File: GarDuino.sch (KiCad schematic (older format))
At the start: 15 parts

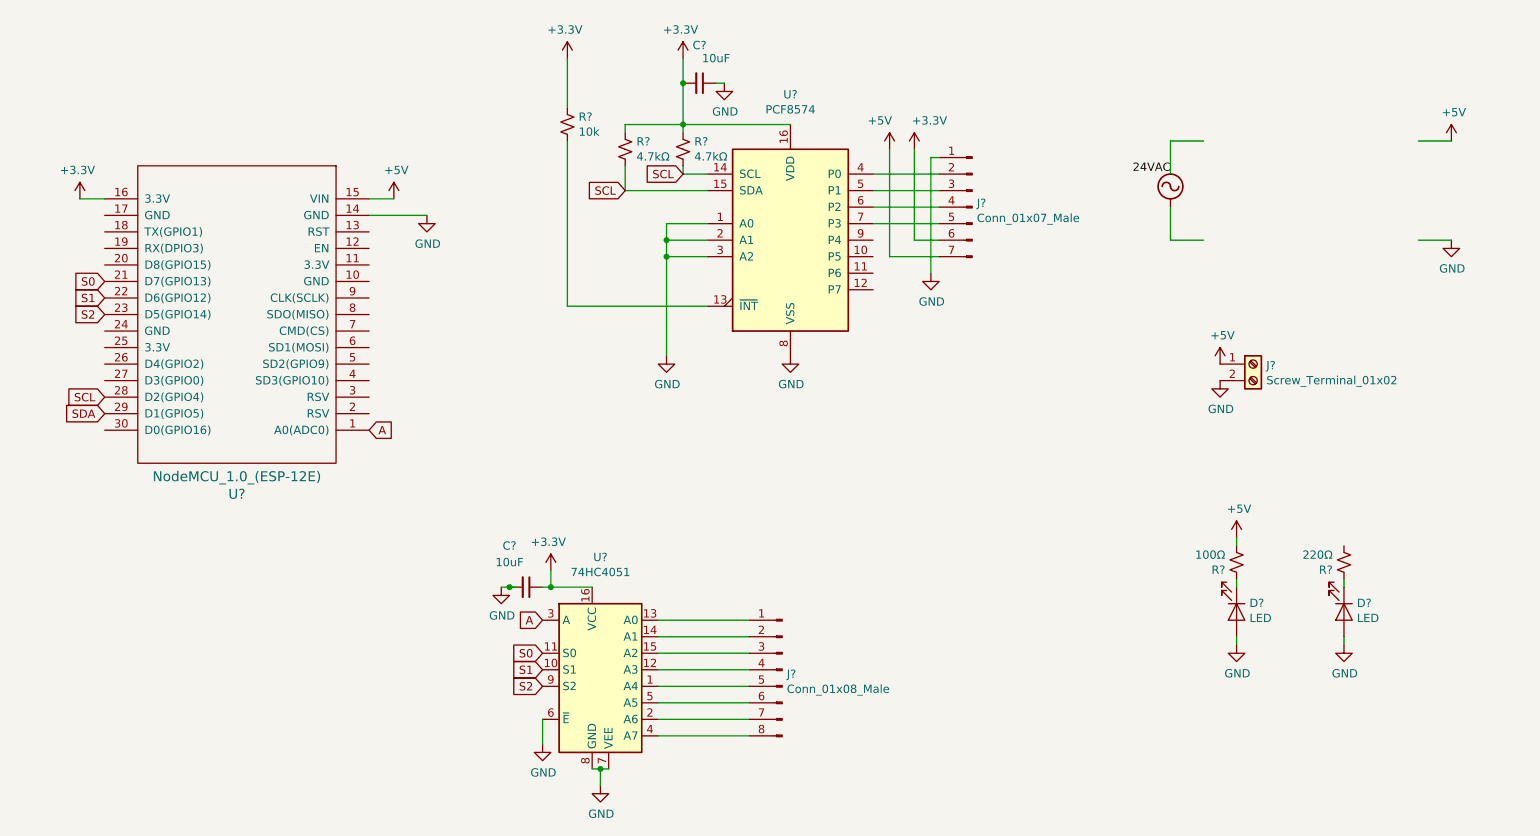
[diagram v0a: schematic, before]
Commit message: Changed schematic to reflect protoboard
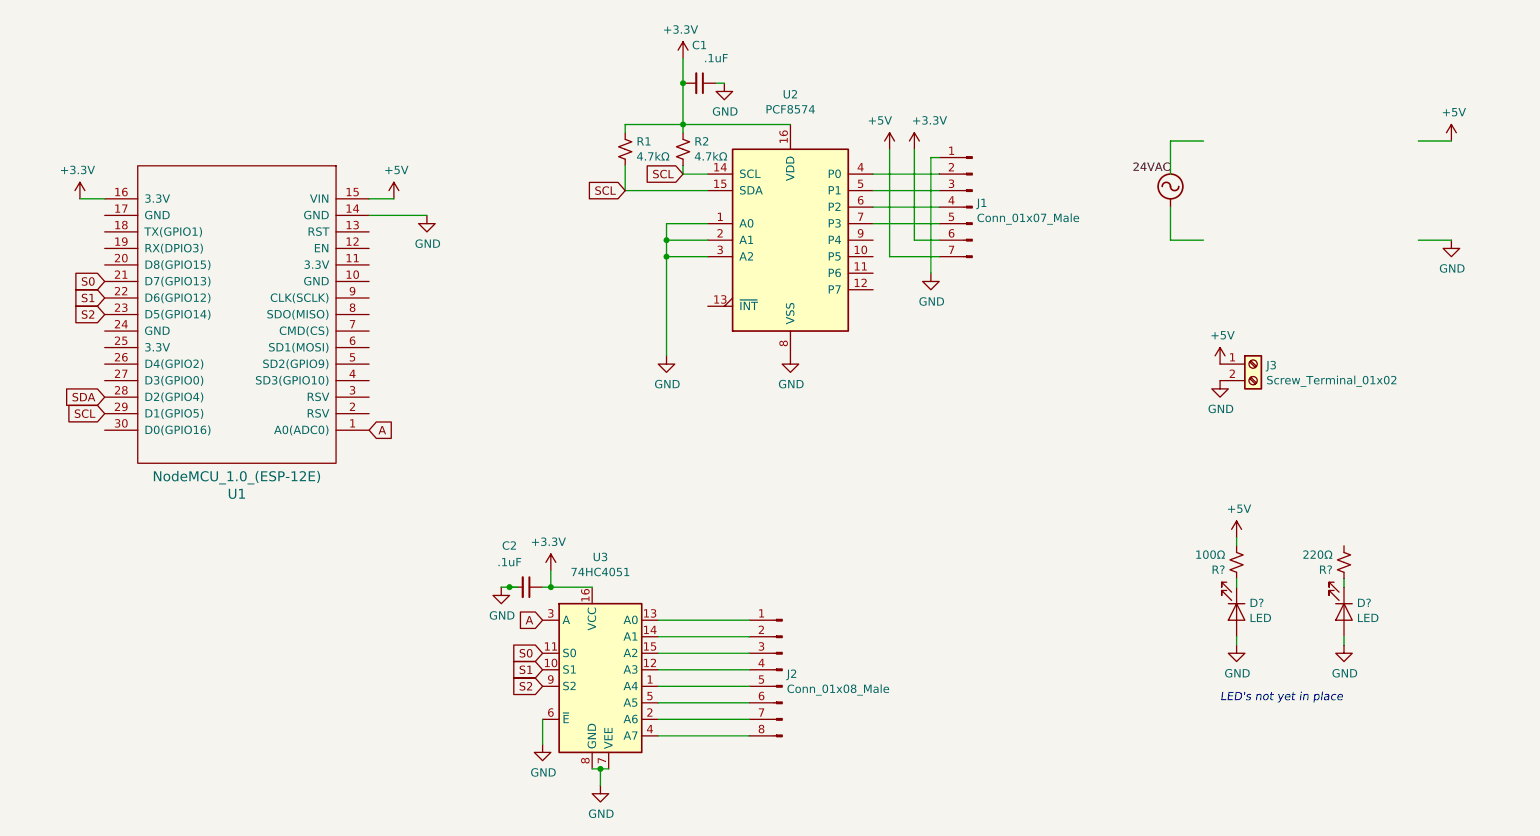
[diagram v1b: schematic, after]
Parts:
- removed R?: 10k, symbol Device:R_Small_US
- C1, C2: renamed from C?; value 10uF -> .1uF
- gave numbers to parts that had none: 8
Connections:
- wire segments 61 -> 58
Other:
- note added: "LED's not yet in place"
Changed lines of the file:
@@
 encoding utf-8
 Sheet 1 1
-Title "Arduino-Based Irrigation Controller"
-Date "2020-04-18"
-Rev "0"
+Title "GarDuino- Arduino-Based Drip Irrigation System"
+Date "2020-04-20"
+Rev "0.1"
 Comp ""
 Comment1 ""
@@
 $EndDescr
 $Comp
-L NodeMCU:NodeMCU_1.0_(ESP-12E) U?
+L NodeMCU:NodeMCU_1.0_(ESP-12E) U1
 U 1 1 5E9944EE
 P 2300 3050
-F 0 "U?" H 2300 4137 60  0000 C CNN
+F 0 "U1" H 2300 4137 60  0000 C CNN
 F 1 "NodeMCU_1.0_(ESP-12E)" H 2300 4031 60  0000 C CNN
 F 2 "" H 1700 2200 60  0000 C CNN
@@
 $EndComp
 $Comp
-L Interface_Expansion:PCF8574 U?
+L Interface_Expansion:PCF8574 U2
 U 1 1 5E99C333
 P 5650 2600
-F 0 "U?" H 5650 3481 50  0000 C CNN
+F 0 "U2" H 5650 3481 50  0000 C CNN
 F 1 "PCF8574" H 5650 3390 50  0000 C CNN
 F 2 "" H 5650 2600 50  0001 C CNN
@@
 $EndComp
 $Comp
-L Device:R_Small_US R?
+L Device:R_Small_US R2
 U 1 1 5E9A68B6
 P 5000 2050
-F 0 "R?" H 5068 2096 50  0000 L CNN
+F 0 "R2" H 5068 2096 50  0000 L CNN
 F 1 "4.7kΩ" H 5068 2005 50  0000 L CNN
 F 2 "" H 5000 2050 50  0001 C CNN
@@
 $EndComp
 $Comp
-L Device:R_Small_US R?
+L Device:R_Small_US R1
 U 1 1 5E9A8484
 P 4650 2050
-F 0 "R?" H 4718 2096 50  0000 L CNN
+F 0 "R1" H 4718 2096 50  0000 L CNN
 F 1 "4.7kΩ" H 4718 2005 50  0000 L CNN
 F 2 "" H 4650 2050 50  0001 C CNN
@@
 	1    0    0    -1
 $EndComp
-$Comp
-L Device:R_Small_US R?
-U 1 1 5E9ABDB9
-P 4300 1900
-F 0 "R?" H 4368 1946 50  0000 L CNN
-F 1 "10k" H 4368 1855 50  0000 L CNN
-F 2 "" H 4300 1900 50  0001 C CNN
-F 3 "~" H 4300 1900 50  0001 C CNN
-	1    4300 1900
-	1    0    0    -1
-$EndComp
 Wire Wire Line
 	4900 2700 4900 3300
@@
 $EndComp
 $Comp
-L 74xx:74HC4051 U?
+L 74xx:74HC4051 U3
 U 1 1 5E9F278B
 P 4450 5200
-F 0 "U?" H 4500 5881 50  0000 C CNN
+F 0 "U3" H 4500 5881 50  0000 C CNN
 F 1 "74HC4051" H 4500 5790 50  0000 C CNN
 F 2 "" H 4450 4800 50  0001 C CNN
@@
 	4200 4700 4450 4700
 $Comp
-L Connector:Conn_01x08_Male J?
+L Connector:Conn_01x08_Male J2
 U 1 1 5E9F7A52
 P 5600 5200
-F 0 "J?" H 5572 5174 50  0000 R CNN
+F 0 "J2" H 5572 5174 50  0000 R CNN
 F 1 "Conn_01x08_Male" H 5572 5083 50  0000 R CNN
 F 2 "" H 5600 5200 50  0001 C CNN
@@
 	-1   0    0    -1
 $EndComp
-$Comp
-L power:+3.3V #PWR?
-U 1 1 5EA082FE
-P 4300 1500
-F 0 "#PWR?" H 4300 1350 50  0001 C CNN
-F 1 "+3.3V" H 4315 1673 50  0000 C CNN
-F 2 "" H 4300 1500 50  0001 C CNN
-F 3 "" H 4300 1500 50  0001 C CNN
-	1    4300 1500
-	-1   0    0    -1
-$EndComp
 Wire Wire Line
 	3450 2450 3100 2450
@@
 	1    0    0    -1
 $EndComp
-Text GLabel 1500 3650 0    50   Input ~ 0
-SDA
 Text GLabel 1500 3550 0    50   Input ~ 0
+SDA
+Text GLabel 1500 3650 0    50   Input ~ 0
 SCL
 Text GLabel 5000 2200 0    50   Input ~ 0
@@
 	5000 1900 5650 1900
 $Comp
-L Device:C_Small C?
+L Device:C_Small C1
 U 1 1 5E9DCD73
 P 5100 1650
-F 0 "C?" V 4871 1650 50  0000 C CNN
-F 1 "10uF" V 4950 1750 50  0000 C CNN
+F 0 "C1" V 4871 1650 50  0000 C CNN
+F 1 ".1uF" V 4950 1750 50  0000 C CNN
 F 2 "" H 5100 1650 50  0001 C CNN
 F 3 "~" H 5100 1650 50  0001 C CNN
@@
 	5000 1650 5000 1900
 $Comp
-L Device:C_Small C?
+L Device:C_Small C2
 U 1 1 5E9E384C
 P 4050 4700
-F 0 "C?" V 3800 4600 50  0000 C CNN
-F 1 "10uF" V 3900 4600 50  0000 C CNN
+F 0 "C2" V 3800 4600 50  0000 C CNN
+F 1 ".1uF" V 3900 4600 50  0000 C CNN
 F 2 "" H 4050 4700 50  0001 C CNN
 F 3 "~" H 4050 4700 50  0001 C CNN
@@
 	6400 2600 6550 2600
 $Comp
-L Connector:Conn_01x07_Male J?
+L Connector:Conn_01x07_Male J1
 U 1 1 5E9E6881
 P 6750 2400
-F 0 "J?" H 6722 2424 50  0000 R CNN
+F 0 "J1" H 6722 2424 50  0000 R CNN
 F 1 "Conn_01x07_Male" H 6722 2333 50  0000 R CNN
 F 2 "" H 6750 2400 50  0001 C CNN
@@
 	-1   0    0    -1
 $EndComp
-Wire Wire Line
-	4300 1500 4300 1800
-Wire Wire Line
-	4300 3000 5150 3000
-Wire Wire Line
-	4300 2000 4300 3000
 $Comp
-L Connector:Screw_Terminal_01x02 J?
+L Connector:Screw_Terminal_01x02 J3
 U 1 1 5E9B783E
 P 8450 3350
-F 0 "J?" H 8530 3342 50  0000 L CNN
+F 0 "J3" H 8530 3342 50  0000 L CNN
 F 1 "Screw_Terminal_01x02" H 8530 3251 50  0000 L CNN
 F 2 "" H 8450 3350 50  0001 C CNN
@@
 	1    0    0    -1
 $EndComp
+Text Notes 8250 5400 0    50   Italic 0
+LED's not yet in place
 $EndSCHEMATC

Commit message: Added headers and connections for peripherals
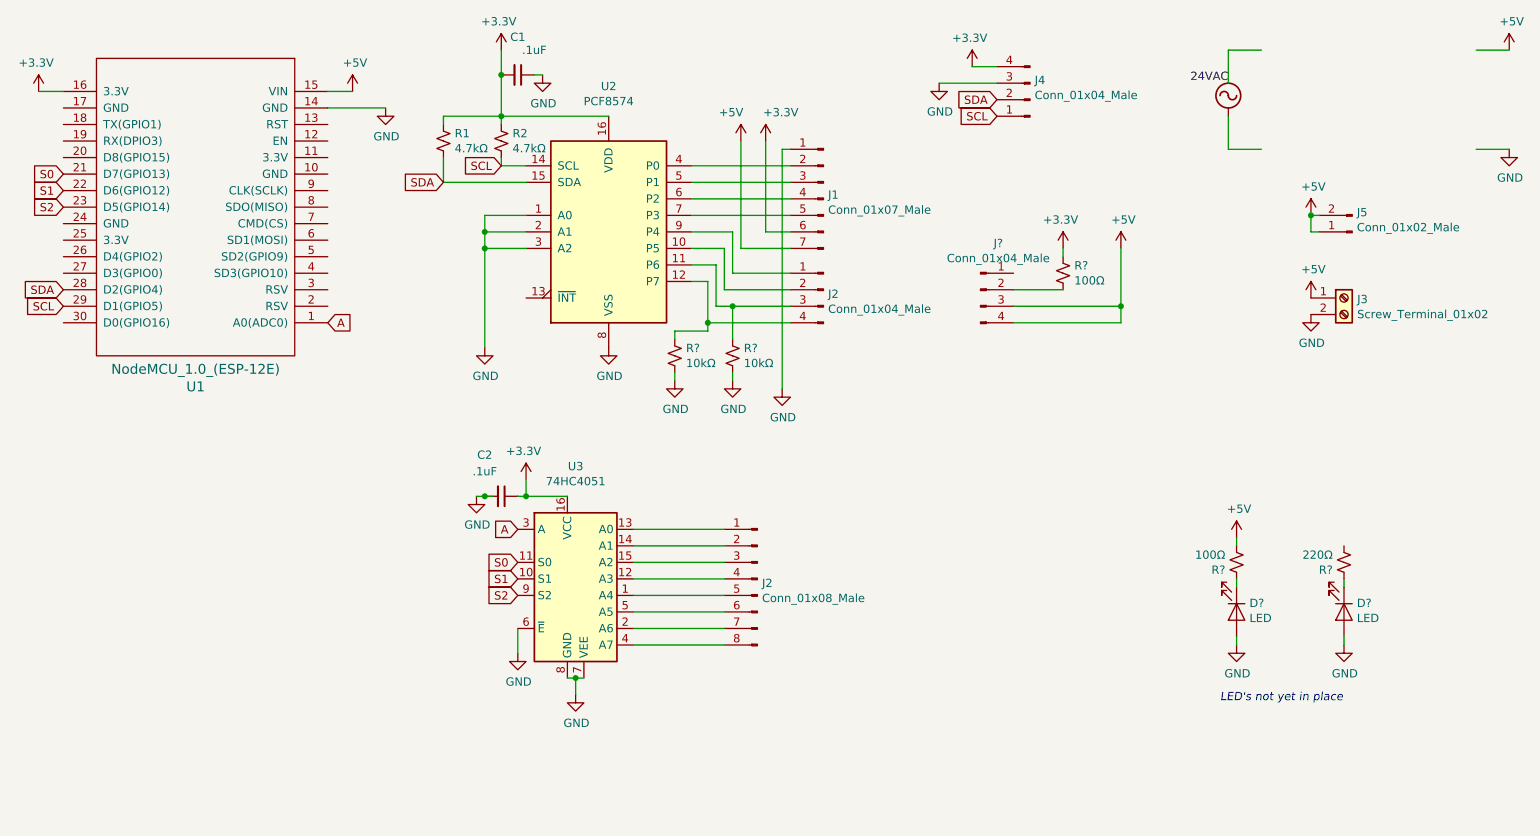
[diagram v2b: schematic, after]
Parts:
- added J2, J4, J?: Conn_01x04_Male, symbol Connector:Conn_01x04_Male
- added J5: Conn_01x02_Male, symbol Connector:Conn_01x02_Male
- added R? (x2): 10kΩ, symbol Device:R_Small_US
- added R?: 100Ω, symbol Device:R_Small_US
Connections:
- wire segments 58 -> 88
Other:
- moved on the sheet: C1, C2, J1, J2, J3, R1, R2, U1, U2, U3
